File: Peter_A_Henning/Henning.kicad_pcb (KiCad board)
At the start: 2 copper layers, 68 x 38 mm, 19 parts, among them P1 RS232, P2 EBUS, Q1 BD645, U1 4011, U2 CNY17-1, U3 78L05, U4 CNY17-1

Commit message: Ditto for Henning's design.
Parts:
- P2: footprint Terminal_Blocks:TerminalBlock_Pheonix_MPT-2.54mm_2pol -> Terminal_Blocks:TerminalBlock_Pheonix_MKDS1.5-2pol
- moved P2 2.55 mm to (73.0, 44.0)
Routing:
- net EBUS1: track 29.8 -> 27.8 mm
- net EBUS2: track 21.1 -> 20.2 mm
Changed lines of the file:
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@@
   (general
     (links 38)
-    (no_connects 0)
-    (area 11.649999 11.649999 80.350002 51.27588)
+    (no_connects 1)
+    (area 11.649999 11.649999 80.350002 51.575)
     (thickness 1.6)
     (drawings 9)
-    (tracks 109)
+    (tracks 111)
     (zones 0)
     (modules 19)
@@
     (visible_elements FFFFFF7F)
     (pcbplotparams
-      (layerselection 0x00000_80000000)
+      (layerselection 0x010f0_80000001)
       (usegerberextensions false)
       (excludeedgelayer true)
@@
       (padsonsilk false)
       (subtractmaskfromsilk false)
-      (outputformat 4)
+      (outputformat 1)
       (mirror false)
-      (drillshape 1)
+      (drillshape 0)
       (scaleselection 1)
       (outputdirectory gerbers))
@@
     )
   )
-  (module Terminal_Blocks:TerminalBlock_Pheonix_MPT-2.54mm_2pol (layer F.Cu)
-    (at 71.2 45.8 180)
-    (descr "2-way 2.54mm pitch terminal block, Phoenix MPT series")
-    (fp_text reference P2 (at 1.27 -4.50088 180) (layer F.SilkS)
-      (effects (font (size 1 1) (thickness 0.15)))
-    )
-    (fp_text value EBUS (at 1.27 4.50088 180) (layer F.Fab)
-      (effects (font (size 1 1) (thickness 0.15)))
-    )
-    (fp_line (start -1.7 -3.3) (end 4.3 -3.3) (layer F.CrtYd) (width 0.05))
-    (fp_line (start -1.7 3.3) (end -1.7 -3.3) (layer F.CrtYd) (width 0.05))
-    (fp_line (start 4.3 3.3) (end -1.7 3.3) (layer F.CrtYd) (width 0.05))
-    (fp_line (start 4.3 -3.3) (end 4.3 3.3) (layer F.CrtYd) (width 0.05))
-    (fp_line (start 4.06908 2.60096) (end -1.52908 2.60096) (layer F.SilkS) (width 0.15))
-    (fp_line (start -1.33096 3.0988) (end -1.33096 2.60096) (layer F.SilkS) (width 0.15))
-    (fp_line (start 3.87096 2.60096) (end 3.87096 3.0988) (layer F.SilkS) (width 0.15))
-    (fp_line (start 1.27 3.0988) (end 1.27 2.60096) (layer F.SilkS) (width 0.15))
-    (fp_line (start -1.52908 -2.70002) (end 4.06908 -2.70002) (layer F.SilkS) (width 0.15))
-    (fp_line (start -1.52908 3.0988) (end 4.06908 3.0988) (layer F.SilkS) (width 0.15))
-    (fp_line (start 4.06908 3.0988) (end 4.06908 -3.0988) (layer F.SilkS) (width 0.15))
-    (fp_line (start 4.06908 -3.0988) (end -1.52908 -3.0988) (layer F.SilkS) (width 0.15))
-    (fp_line (start -1.52908 -3.0988) (end -1.52908 3.0988) (layer F.SilkS) (width 0.15))
-    (pad 2 thru_hole oval (at 2.54 0 180) (size 1.99898 1.99898) (drill 1.09728) (layers *.Cu *.Mask F.SilkS)
+  (module Terminal_Blocks:TerminalBlock_Pheonix_MKDS1.5-2pol (layer F.Cu)
+    (at 73 44 180)
+    (descr "2-way 5mm pitch terminal block, Phoenix MKDS series")
+    (fp_text reference P2 (at 2.5 5.9 180) (layer F.SilkS)
+      (effects (font (size 1 1) (thickness 0.15)))
+    )
+    (fp_text value EBUS (at 2.5 -6.6 180) (layer F.Fab)
+      (effects (font (size 1 1) (thickness 0.15)))
+    )
+    (fp_line (start -2.7 -5.4) (end 7.7 -5.4) (layer F.CrtYd) (width 0.05))
+    (fp_line (start -2.7 4.8) (end -2.7 -5.4) (layer F.CrtYd) (width 0.05))
+    (fp_line (start 7.7 4.8) (end -2.7 4.8) (layer F.CrtYd) (width 0.05))
+    (fp_line (start 7.7 -5.4) (end 7.7 4.8) (layer F.CrtYd) (width 0.05))
+    (fp_line (start 2.5 4.1) (end 2.5 4.6) (layer F.SilkS) (width 0.15))
+    (fp_circle (center 5 0.1) (end 3 0.1) (layer F.SilkS) (width 0.15))
+    (fp_circle (center 0 0.1) (end 2 0.1) (layer F.SilkS) (width 0.15))
+    (fp_line (start -2.5 2.6) (end 7.5 2.6) (layer F.SilkS) (width 0.15))
+    (fp_line (start -2.5 -2.3) (end 7.5 -2.3) (layer F.SilkS) (width 0.15))
+    (fp_line (start -2.5 4.1) (end 7.5 4.1) (layer F.SilkS) (width 0.15))
+    (fp_line (start -2.5 4.6) (end 7.5 4.6) (layer F.SilkS) (width 0.15))
+    (fp_line (start 7.5 4.6) (end 7.5 -5.2) (layer F.SilkS) (width 0.15))
+    (fp_line (start 7.5 -5.2) (end -2.5 -5.2) (layer F.SilkS) (width 0.15))
+    (fp_line (start -2.5 -5.2) (end -2.5 4.6) (layer F.SilkS) (width 0.15))
+    (pad 1 thru_hole rect (at 0 0 180) (size 2.5 2.5) (drill 1.3) (layers *.Cu *.Mask F.SilkS)
+      (net 4 EBUS2))
+    (pad 2 thru_hole circle (at 5 0 180) (size 2.5 2.5) (drill 1.3) (layers *.Cu *.Mask F.SilkS)
       (net 3 EBUS1))
-    (pad 1 thru_hole rect (at 0 0 180) (size 1.99898 1.99898) (drill 1.09728) (layers *.Cu *.Mask F.SilkS)
-      (net 4 EBUS2))
-    (model Terminal_Blocks.3dshapes/TerminalBlock_Pheonix_MPT-2.54mm_2pol.wrl
-      (at (xyz 0.05 0 0))
+    (model Terminal_Blocks.3dshapes/TerminalBlock_Pheonix_MKDS1.5-2pol.wrl
+      (at (xyz 0.0984 0 0))
       (scale (xyz 1 1 1))
       (rotate (xyz 0 0 0))
@@
   (segment (start 16.46 20) (end 16.46 24) (width 0.3) (layer B.Cu) (net 2))
   (segment (start 16.46 24) (end 18.96 26.5) (width 0.3) (layer B.Cu) (net 2))
-  (segment (start 68.66 45.8) (end 68.66 44.76) (width 0.3) (layer B.Cu) (net 3))
+  (segment (start 68 44) (end 66.750001 42.750001) (width 0.3) (layer B.Cu) (net 3))
+  (segment (start 66.750001 42.750001) (end 66.650001 42.750001) (width 0.3) (layer B.Cu) (net 3))
+  (segment (start 66.650001 42.750001) (end 60.6 36.7) (width 0.3) (layer B.Cu) (net 3))
   (segment (start 60.6 28.39798) (end 63.00052 25.99746) (width 0.3) (layer B.Cu) (net 3))
   (segment (start 60.6 36.7) (end 60.6 28.39798) (width 0.3) (layer B.Cu) (net 3))
-  (segment (start 68.66 44.76) (end 60.6 36.7) (width 0.3) (layer B.Cu) (net 3))
   (segment (start 65.83948 21.50254) (end 65.83948 23.1585) (width 0.3) (layer B.Cu) (net 3))
   (segment (start 65.83948 23.1585) (end 63.00052 25.99746) (width 0.3) (layer B.Cu) (net 3))
-  (segment (start 71.2 45.8) (end 71.2 39.9) (width 0.3) (layer B.Cu) (net 4))
-  (segment (start 71.2 39.9) (end 65.79746 34.49746) (width 0.3) (layer B.Cu) (net 4))
+  (segment (start 73 44) (end 73 42.45) (width 0.3) (layer B.Cu) (net 4))
+  (segment (start 73 42.45) (end 65.83948 35.28948) (width 0.3) (layer B.Cu) (net 4))
+  (segment (start 65.83948 35.28948) (end 65.83948 34.33948) (width 0.3) (layer B.Cu) (net 4))
   (segment (start 63.00052 34.49746) (end 65.79746 34.49746) (width 0.3) (layer B.Cu) (net 4))
   (segment (start 65.79746 34.49746) (end 65.99746 34.49746) (width 0.3) (layer B.Cu) (net 4))

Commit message: Generated some gerbers.
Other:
- board text added: "eBUS Adapter"
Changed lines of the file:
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@@
   (general
     (links 38)
-    (no_connects 1)
-    (area 11.649999 11.649999 80.350002 51.575)
+    (no_connects 0)
+    (area 11.924999 11.924999 80.075001 50.075001)
     (thickness 1.6)
-    (drawings 9)
+    (drawings 10)
     (tracks 111)
     (zones 0)
@@
     )
   )
+  (gr_text "eBUS Adapter" (at 23 14.25) (layer B.Cu)
+    (effects (font (size 1.5 1.5) (thickness 0.3)) (justify mirror))
+  )
   (gr_line (start 38.5 50) (end 39 50) (angle 90) (layer Edge.Cuts) (width 0.15))

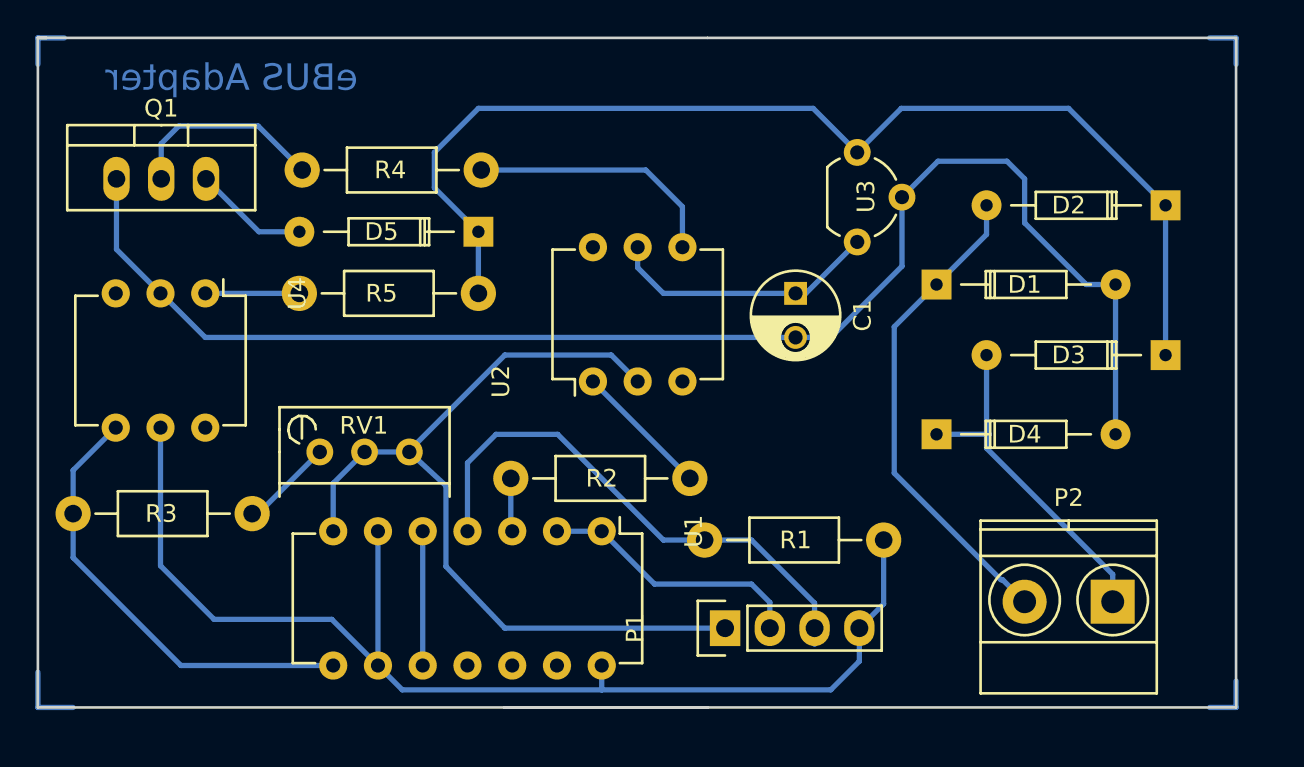
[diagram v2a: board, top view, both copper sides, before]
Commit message: Fixed a silly error - reversed some polarities, no wonder this whole thing didn't work.
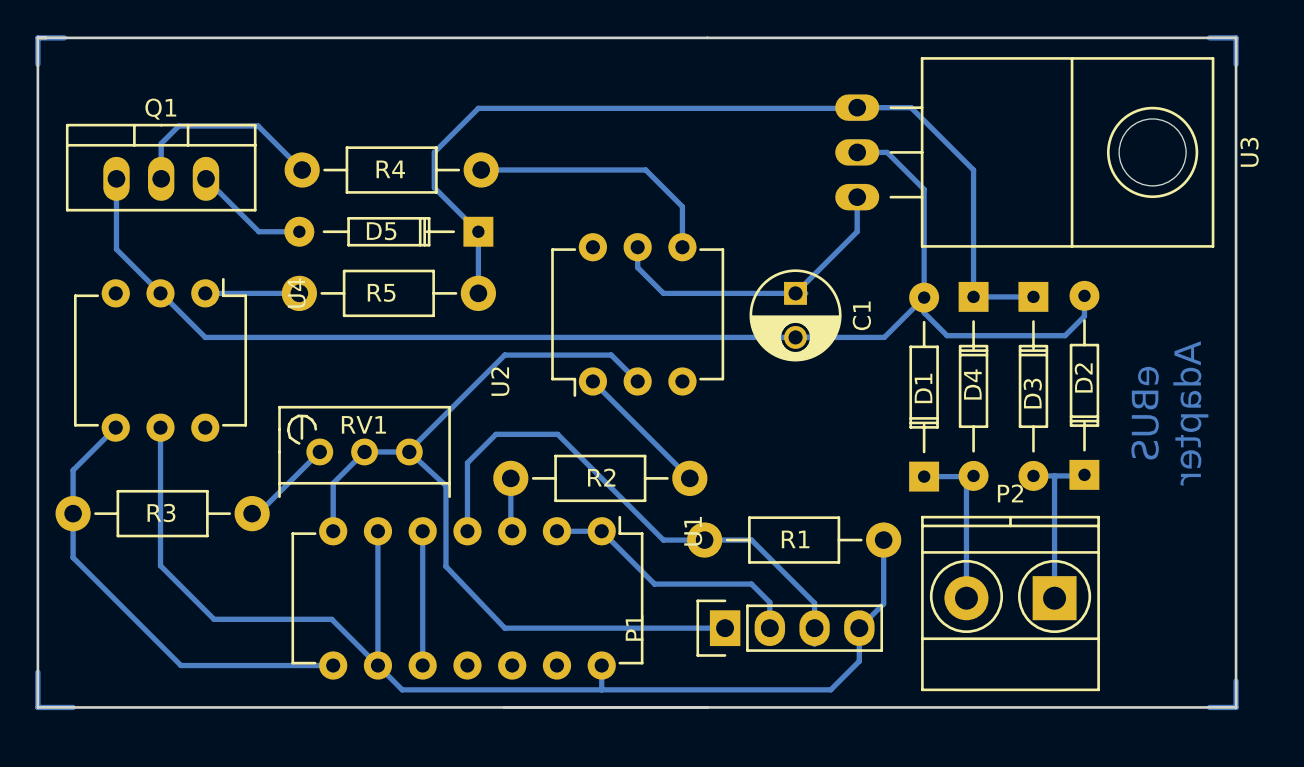
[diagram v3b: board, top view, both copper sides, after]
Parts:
- U3: footprint TO_SOT_Packages_THT:TO-92_Molded_Wide -> TO_SOT_Packages_THT:TO-220_Neutral123_Horizontal
- moved D2 16.0 mm to (71.4, 36.8), turned to 90 degrees
- moved D1 10.9 mm to (62.3, 36.9), turned to 90 degrees
- moved D3 8.19 mm to (68.5, 26.7), turned to 270 degrees
- moved D4 8.08 mm to (65.1, 26.7), turned to 270 degrees
- moved P2 3.31 mm to (69.7, 43.8)
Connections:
- D2 pad 1: Net-(D2-Pad1) -> EBUS2
- D2 pad 2: EBUS1 -> Net-(C1-Pad2)
- D3 pad 1: Net-(D2-Pad1) -> Net-(D3-Pad1)
- D4 pad 1: EBUS2 -> Net-(D3-Pad1)
- D4 pad 2: Net-(C1-Pad2) -> EBUS1
- D5 pad 1: Net-(D2-Pad1) -> Net-(D3-Pad1)
- R5 pad 1: Net-(D2-Pad1) -> Net-(D3-Pad1)
- U3 pad 1: Net-(D2-Pad1) -> Net-(D3-Pad1)
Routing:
- net Net-(D2-Pad1): track 64.4 -> 0.00 mm
- net Net-(D3-Pad1): track 0.00 -> 52.8 mm
- net EBUS1: track 27.8 -> 9.93 mm
- net EBUS2: track 20.2 -> 9.86 mm
- net Net-(C1-Pad2): track 82.1 -> 78.3 mm
- net Net-(C1-Pad1): track 15.4 -> 18.2 mm

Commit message: Added a LED, regenerated production files.
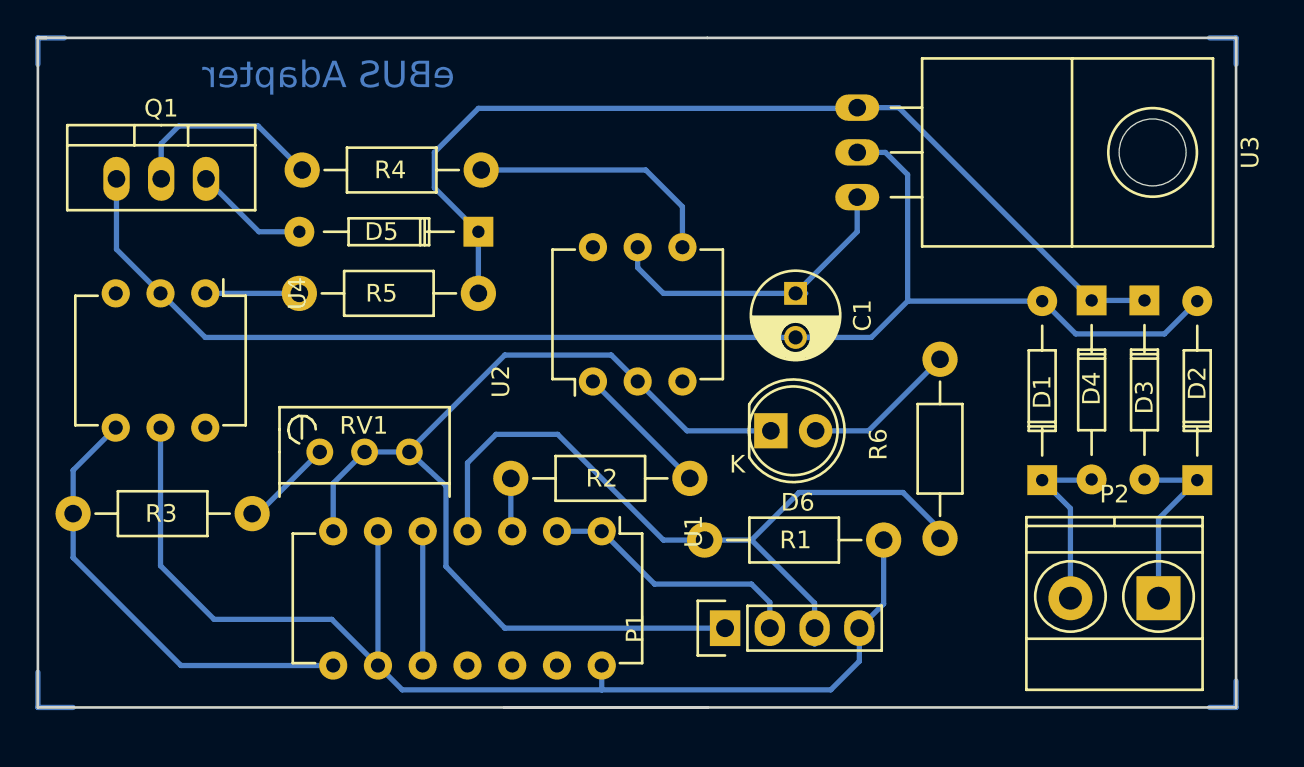
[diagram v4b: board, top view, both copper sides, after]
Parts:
- added D6: LED, LEDs:LED-5MM, F.Cu at (53.6, 34.3)
- added R6: 1k, Resistors_ThroughHole:Resistor_Horizontal_RM10mm, F.Cu at (63.2, 40.4)
- moved D1 6.70 mm to (69.0, 37.1)
- moved D4 6.70 mm to (71.8, 26.9)
- moved D2 6.41 mm to (77.8, 37.1)
- moved D3 6.30 mm to (74.8, 26.9)
- moved P2 5.90 mm to (75.6, 43.8)
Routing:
- net RXD: track 30.6 -> 43.7 mm
- net Net-(D6-Pad2): track 0.00 -> 8.74 mm
- net GND: track 48.5 -> 57.3 mm
- net Net-(C1-Pad2): track 78.3 -> 82.4 mm
- net Net-(D3-Pad1): track 52.8 -> 54.9 mm
- net EBUS2: track 9.86 -> 10.6 mm
